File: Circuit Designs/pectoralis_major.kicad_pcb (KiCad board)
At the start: 4 copper layers, 100 x 100 mm, 293 parts, among them J1 0524651671, J2 0533071071, J3 0533071071, J4 0524651071, J5 SoicBite, Q1 AO3400A, Q2 AO3400A, Q3 BUK7V4R2, Q4 BUK7V4R2, Q5 BUK7V4R2, T1 B3380, T2 B3380, U1 TCAN330, U10 INA199A1, U11 AS5047P, U2 STM32F405RGTx, U3 AP2127, U4 AP2127, U5 AP2127, U6 AP2127, U7 DRV8301, U8 INA199A1, U9 INA199A1, Y1 CSTNE8M00

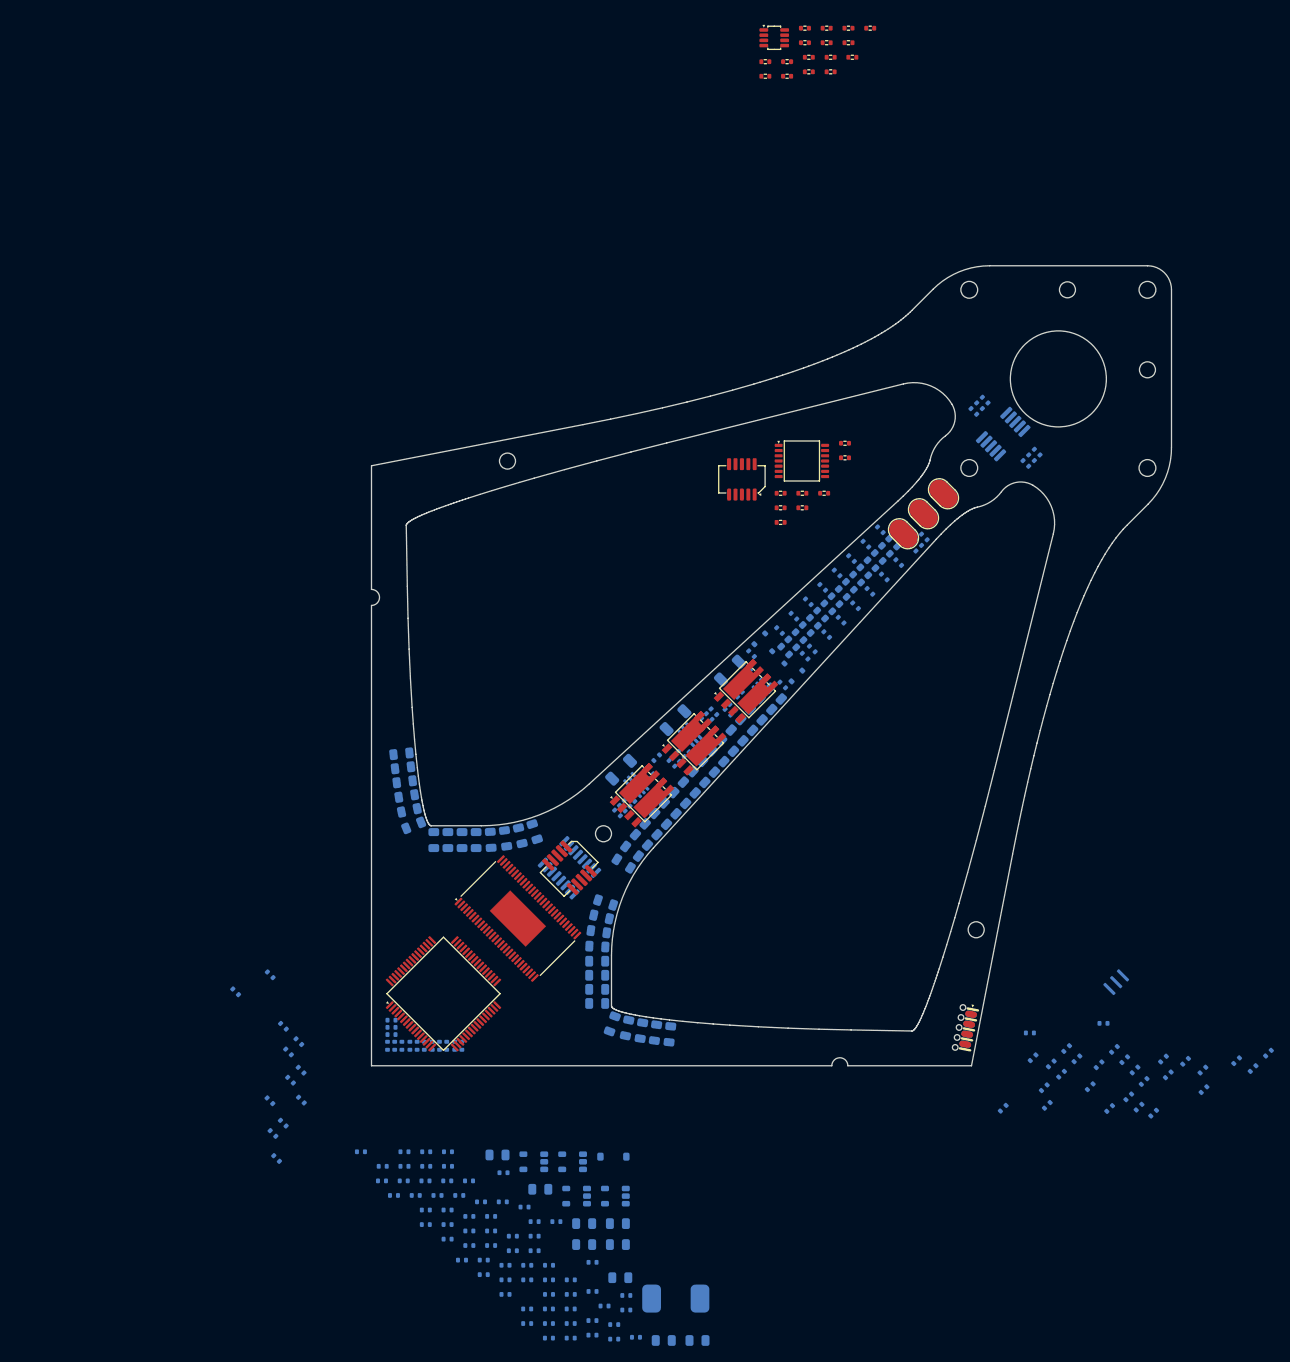
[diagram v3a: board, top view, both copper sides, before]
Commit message: First placement of the MCU Page's components are done
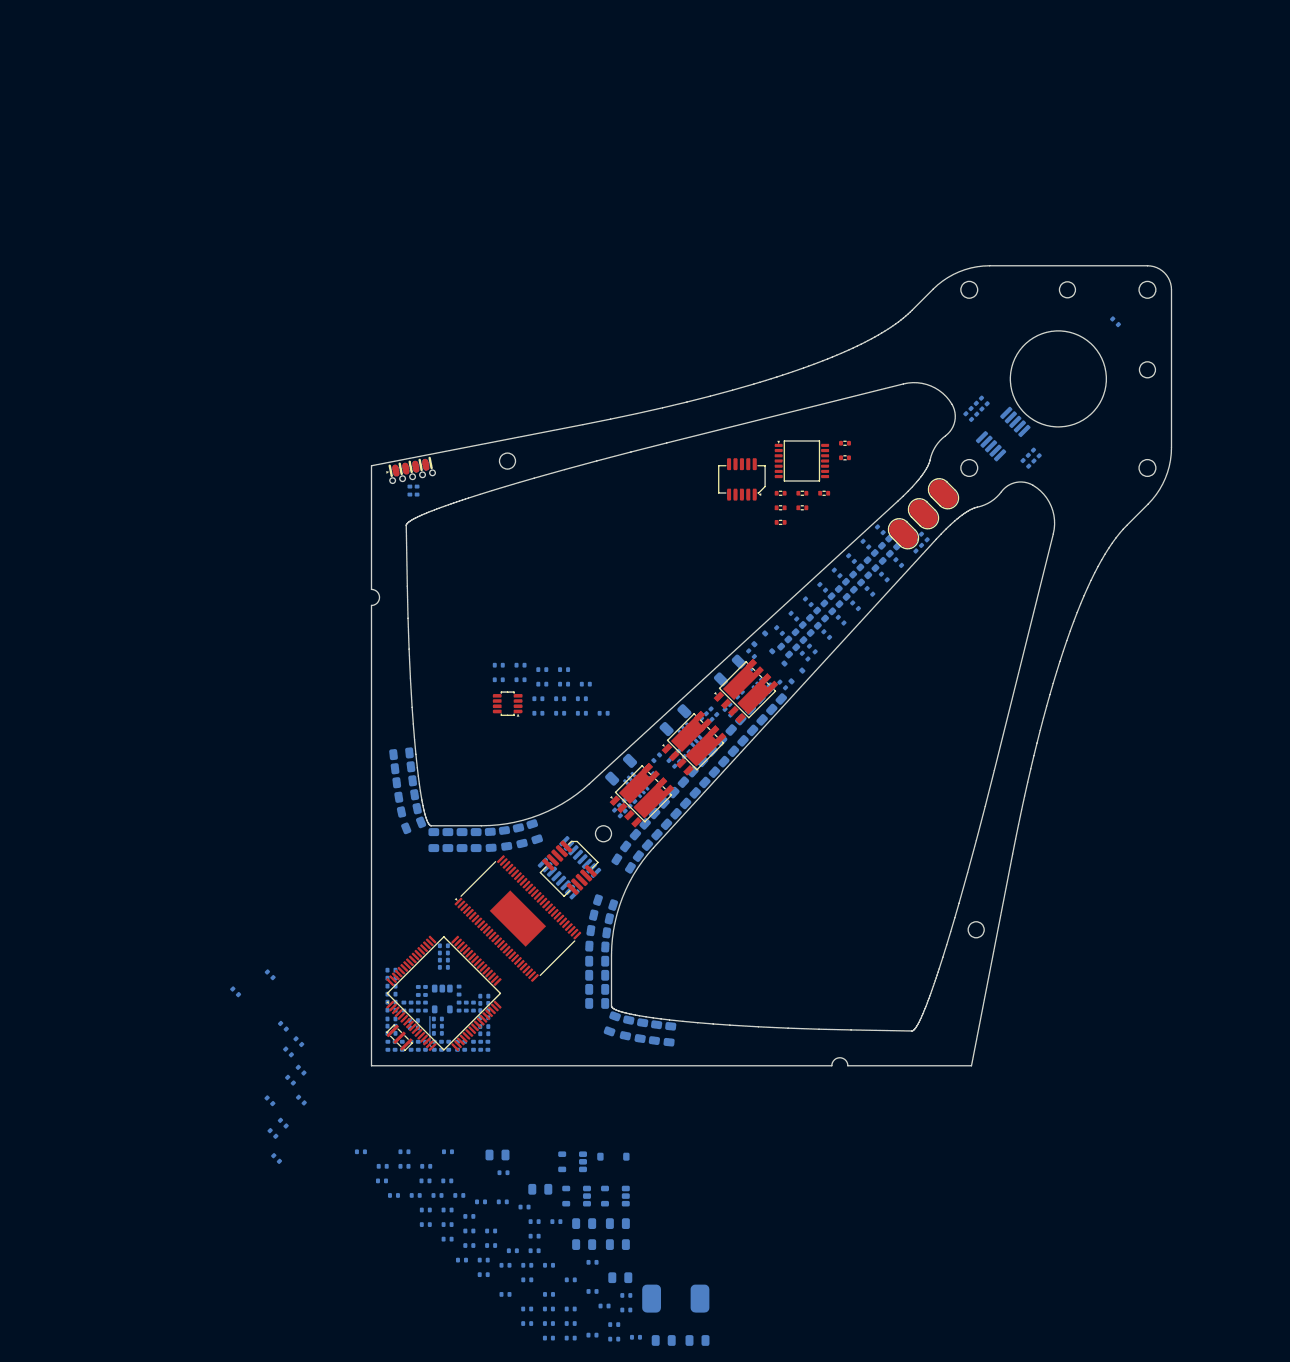
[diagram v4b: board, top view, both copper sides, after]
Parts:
- C27, C28, C29, C30, C31, C32, C33, R1, R2, R3, R4, R5, R6, R7, R8, R9: moved to B.Cu
- Y1: moved to F.Cu
- moved R13 108.6 mm to (105.7, 78.1), turned to 90 degrees
- moved R12 103.0 mm to (104.8, 78.1), turned to -90 degrees
- moved C47 102.1 mm to (102.5, 139.1), turned to 180 degrees
- moved C49 102.0 mm to (108.3, 145.9), turned to 0 degrees
- moved J5 100.1 mm to (104.8, 74.5), turned to -169 degrees
- moved C43 100.0 mm to (109.0, 135.9), turned to 180 degrees
- moved C39 97.6 mm to (114.5, 147.5), turned to -90 degrees
- moved C35 96.8 mm to (102.5, 142.1), turned to 180 degrees
- moved T1 95.7 mm to (193.0, 57.0), turned to 135 degrees
- moved C36 94.7 mm to (102.5, 141.1), turned to 180 degrees
- moved C48 93.8 mm to (102.5, 138.1), turned to 180 degrees
- moved C29 91.9 mm to (126.3, 105.9)
- moved C33 91.9 mm to (123.6, 105.9)
- moved R5 91.9 mm to (120.9, 105.9)
- moved R6 91.9 mm to (129.0, 105.9)
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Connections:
- C76 pad 1: +5V -> +5VA
- C77 pad 1: +5V -> +5VA
- C78 pad 1: +5V -> +5VA
- C79 pad 1: +5V -> +5VA
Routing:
- net /powerDrivers/SH_C: track 0.00 -> 4.38 mm

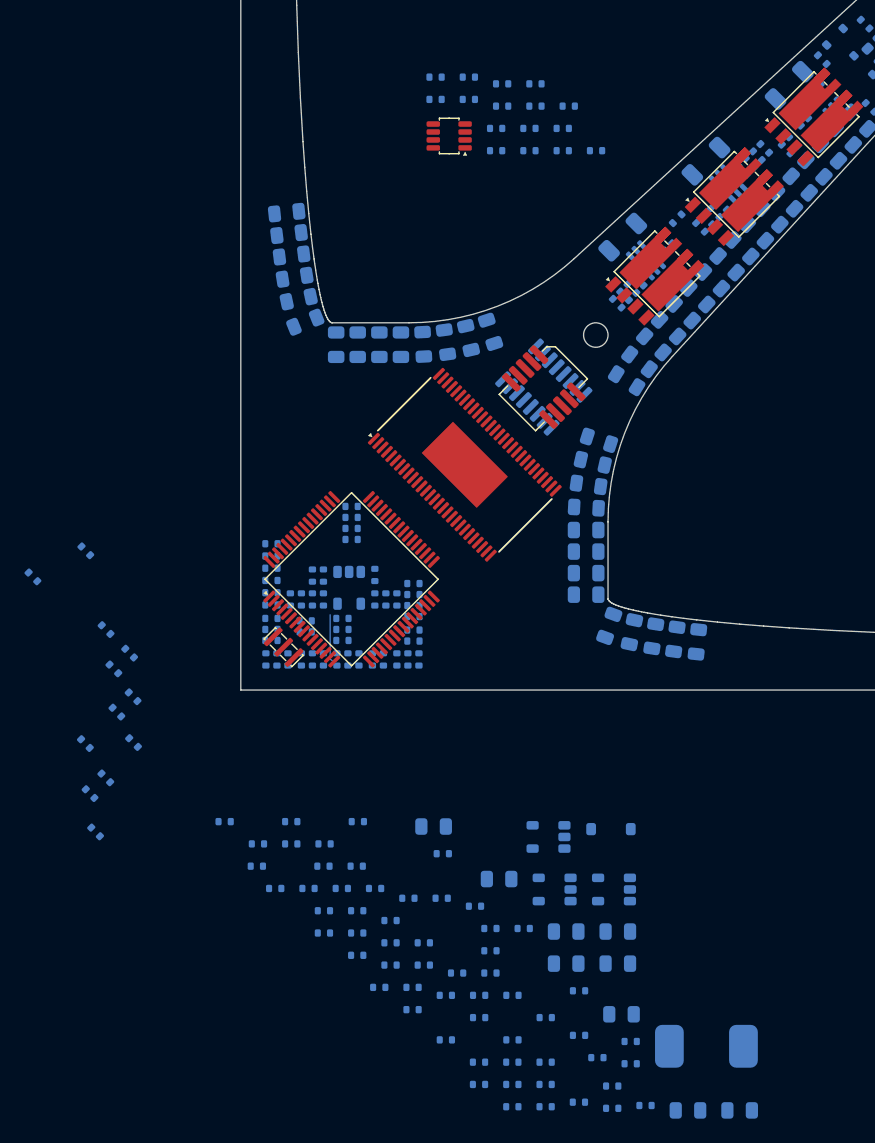
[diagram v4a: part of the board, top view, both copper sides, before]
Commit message: placing all the regulators are done
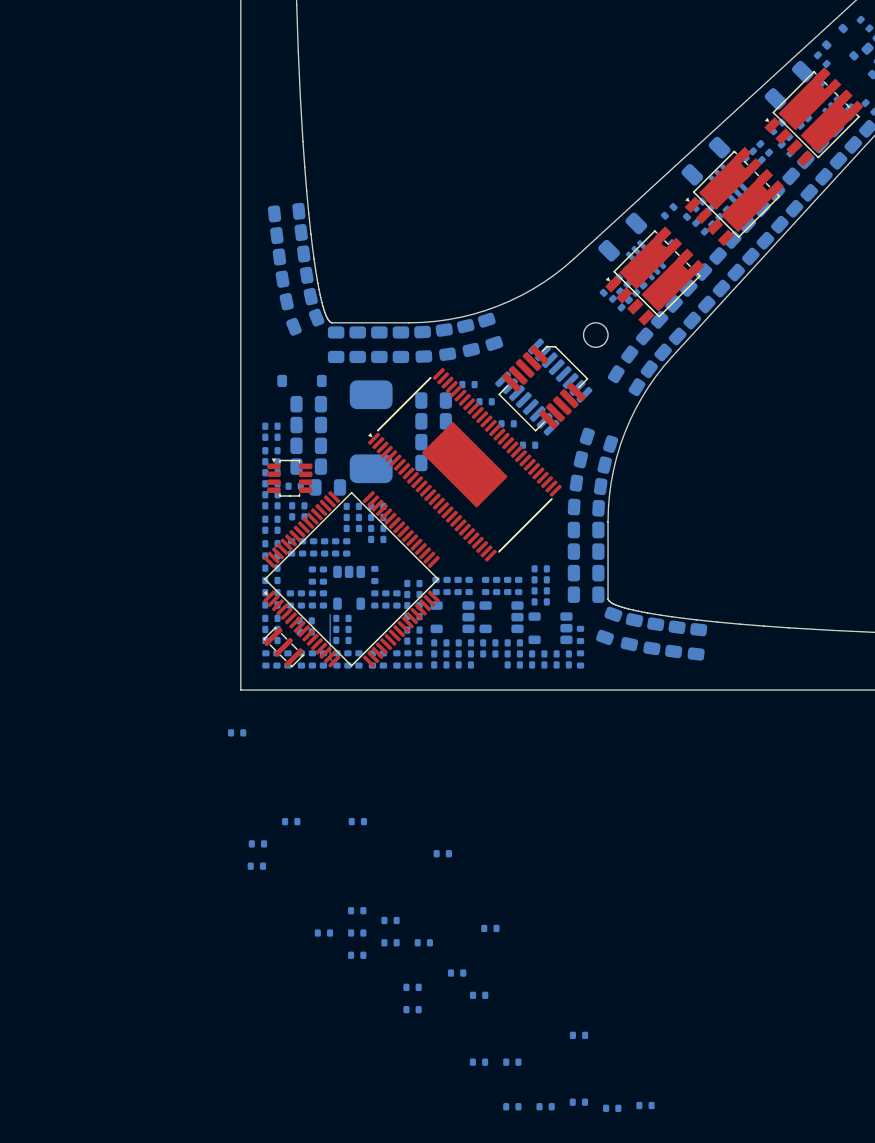
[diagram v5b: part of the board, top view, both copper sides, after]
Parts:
- moved R80 72.1 mm to (143.8, 104.0), turned to -135 degrees
- moved R77 72.0 mm to (145.1, 102.8), turned to -135 degrees
- moved R78 68.2 mm to (138.1, 109.8), turned to -135 degrees
- moved C81 61.6 mm to (115.8, 126.3), turned to 0 degrees
- moved C88 61.0 mm to (107.1, 133.4), turned to 0 degrees
- moved R81 58.7 mm to (136.8, 111.0), turned to -135 degrees
- moved R79 58.4 mm to (131.2, 116.0), turned to -135 degrees
- moved L1 57.2 mm to (110.7, 128.9), turned to 90 degrees
- moved C99 55.8 mm to (120.0, 126.5), turned to 0 degrees
- moved C84 53.0 mm to (105.5, 130.1), turned to 0 degrees
- moved C80 52.2 mm to (105.5, 126.7), turned to 0 degrees
- moved R82 47.7 mm to (130.0, 117.2), turned to -135 degrees
- moved C105 47.2 mm to (121.8, 128.2), turned to 0 degrees
- moved C82 46.4 mm to (105.5, 128.3), turned to 0 degrees
- moved C86 45.6 mm to (105.5, 131.8), turned to 0 degrees
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
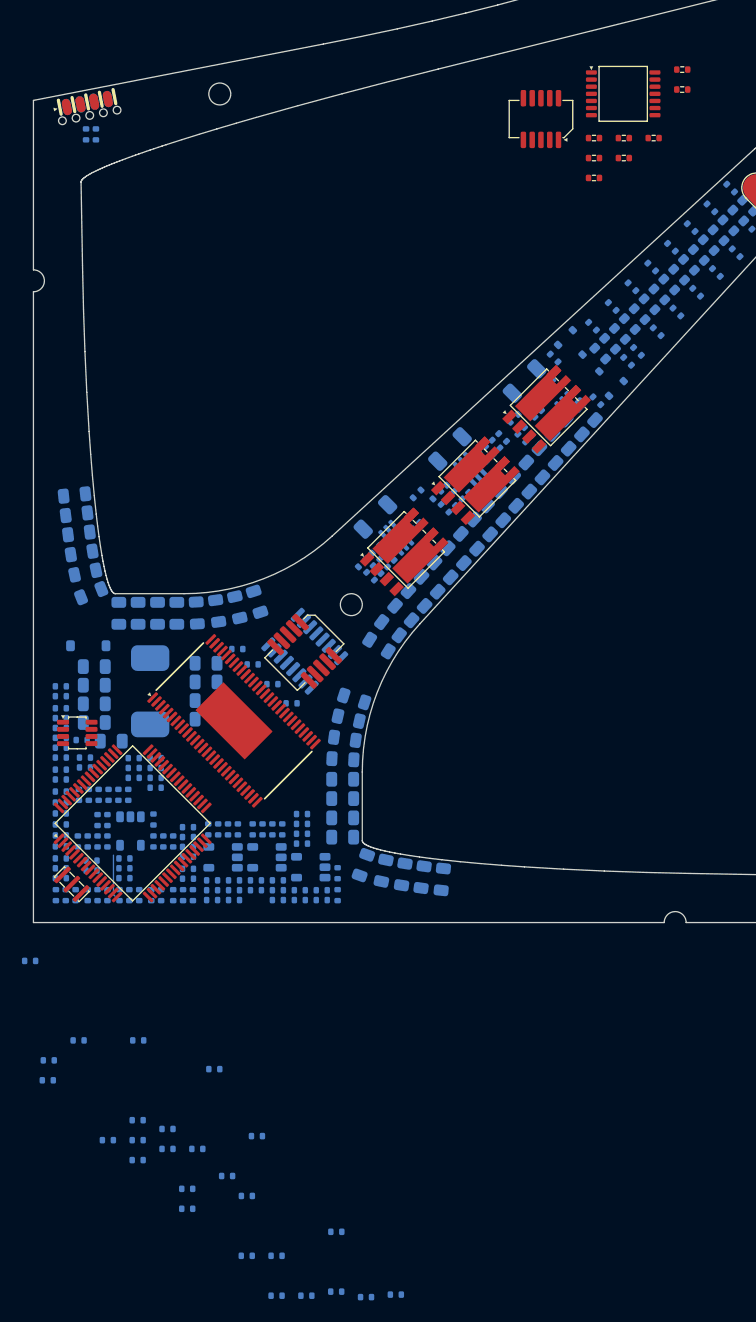
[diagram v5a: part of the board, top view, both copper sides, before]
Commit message: placed all the components except magnetic sensor board
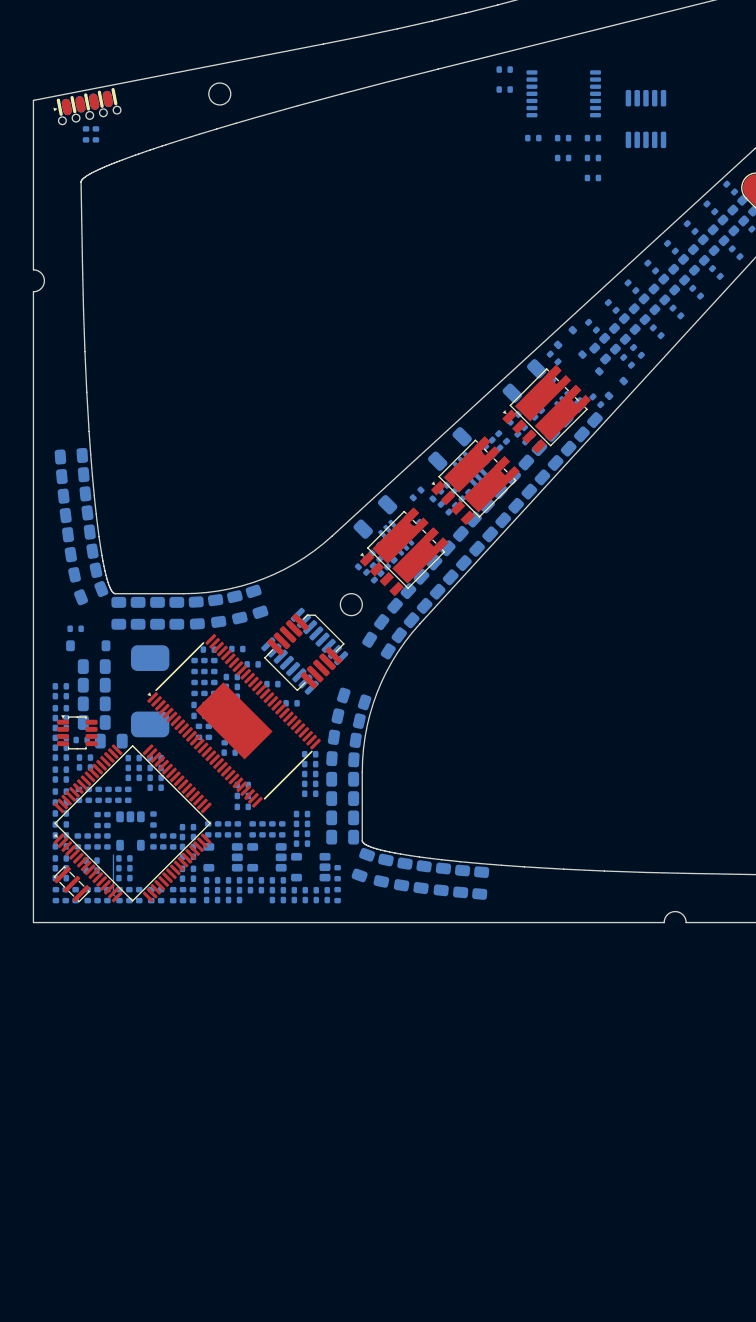
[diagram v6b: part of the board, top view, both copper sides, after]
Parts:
- C154, C155, C156, C157, J4, R87, R88, R89, R90, U11: moved to B.Cu
- moved C90 59.7 mm to (116.5, 126.6), turned to -90 degrees
- moved R51 57.3 mm to (116.5, 128.6), turned to 90 degrees
- moved R56 55.0 mm to (115.2, 130.2)
- moved R54 53.0 mm to (115.6, 126.6), turned to 90 degrees
- moved R60 49.7 mm to (115.2, 131.2)
- moved R61 46.9 mm to (119.1, 137.4), turned to 0 degrees
- moved R53 46.6 mm to (114.7, 128.6), turned to 90 degrees
- moved C104 45.9 mm to (125.2, 138.2)
- moved C101 45.2 mm to (125.2, 135.6)
- moved C92 44.6 mm to (116.0, 125.1)
- moved R52 44.6 mm to (115.6, 128.6), turned to -90 degrees
- moved C97 43.1 mm to (117.5, 133.1), turned to -90 degrees
- moved C106 41.7 mm to (118.1, 129.4), turned to 0 degrees
- moved C100 41.2 mm to (125.2, 134.7)
- moved C107 40.8 mm to (118.1, 128.5), turned to 0 degrees
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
